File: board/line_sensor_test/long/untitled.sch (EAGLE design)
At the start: 12 parts

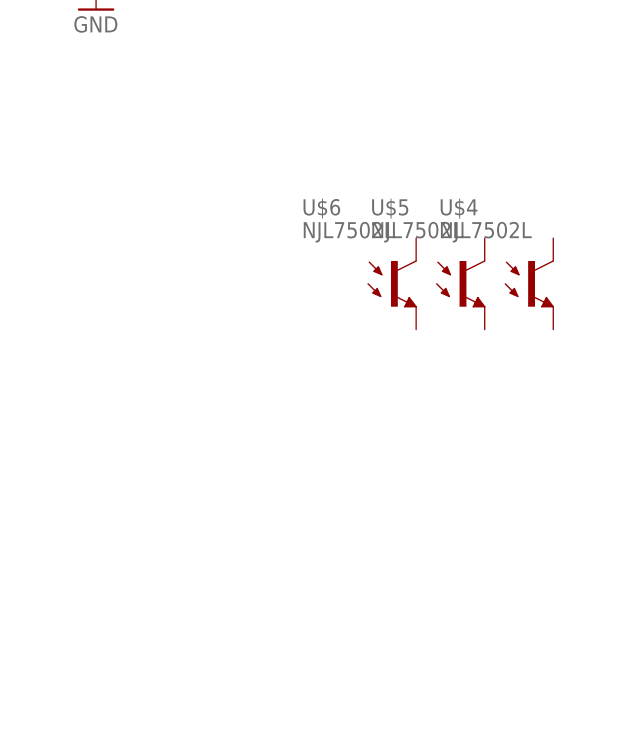
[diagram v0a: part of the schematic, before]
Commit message: add long line sensor
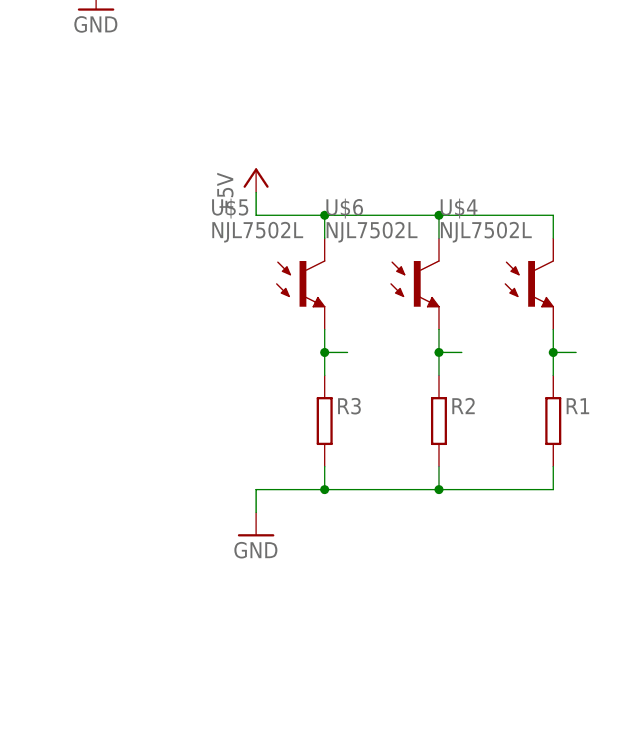
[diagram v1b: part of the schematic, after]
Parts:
- added R1, R2, R3: (no value), generic:RESISTOR1608
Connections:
- new net N$10: R1.1, U$4.E
- new net N$11: R3.1, U$5.E
- new net N$9: R2.1, U$6.E
- net +5V: now also U$4.C, U$5.C, U$6.C
- net GND: now also R1.2, R2.2, R3.2
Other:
- moved on the sheet: U$5, U$6
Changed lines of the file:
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@@
 <part name="LED6" library="adafruit" deviceset="WS2812B" device="_5050N"/>
 <part name="GND2" library="supply1" library_urn="urn:adsk.eagle:library:371" deviceset="GND" device=""/>
+<part name="R1" library="generic" deviceset="RESISTOR" device="1608"/>
+<part name="R2" library="generic" deviceset="RESISTOR" device="1608"/>
+<part name="R3" library="generic" deviceset="RESISTOR" device="1608"/>
+<part name="P+2" library="supply1" library_urn="urn:adsk.eagle:library:371" deviceset="+5V" device=""/>
+<part name="GND3" library="supply1" library_urn="urn:adsk.eagle:library:371" deviceset="GND" device=""/>
 </parts>
 <sheets>
@@
 <attribute name="VALUE" x="88.9" y="63.5" size="1.778" layer="96"/>
 </instance>
-<instance part="U$5" gate="G$1" x="91.44" y="58.42" smashed="yes">
-<attribute name="NAME" x="81.28" y="66.04" size="1.778" layer="95"/>
-<attribute name="VALUE" x="81.28" y="63.5" size="1.778" layer="96"/>
-</instance>
-<instance part="U$6" gate="G$1" x="83.82" y="58.42" smashed="yes">
-<attribute name="NAME" x="73.66" y="66.04" size="1.778" layer="95"/>
-<attribute name="VALUE" x="73.66" y="63.5" size="1.778" layer="96"/>
+<instance part="U$5" gate="G$1" x="73.66" y="58.42" smashed="yes">
+<attribute name="NAME" x="63.5" y="66.04" size="1.778" layer="95"/>
+<attribute name="VALUE" x="63.5" y="63.5" size="1.778" layer="96"/>
+</instance>
+<instance part="U$6" gate="G$1" x="86.36" y="58.42" smashed="yes">
+<attribute name="NAME" x="76.2" y="66.04" size="1.778" layer="95"/>
+<attribute name="VALUE" x="76.2" y="63.5" size="1.778" layer="96"/>
 </instance>
 <instance part="LED6" gate="G$1" x="-33.02" y="106.68" smashed="yes"/>
 <instance part="GND2" gate="1" x="50.8" y="88.9" smashed="yes">
 <attribute name="VALUE" x="48.26" y="86.36" size="1.778" layer="96"/>
+</instance>
+<instance part="R1" gate="G$1" x="101.6" y="43.18" smashed="yes">
+<attribute name="NAME" x="102.87" y="45.72" size="1.778" layer="95" font="vector" rot="MR180"/>
+<attribute name="VALUE" x="102.87" y="40.64" size="1.778" layer="96" font="vector"/>
+</instance>
+<instance part="R2" gate="G$1" x="88.9" y="43.18" smashed="yes">
+<attribute name="NAME" x="90.17" y="45.72" size="1.778" layer="95" font="vector" rot="MR180"/>
+<attribute name="VALUE" x="90.17" y="40.64" size="1.778" layer="96" font="vector"/>
+</instance>
+<instance part="R3" gate="G$1" x="76.2" y="43.18" smashed="yes">
+<attribute name="NAME" x="77.47" y="45.72" size="1.778" layer="95" font="vector" rot="MR180"/>
+<attribute name="VALUE" x="77.47" y="40.64" size="1.778" layer="96" font="vector"/>
+</instance>
+<instance part="P+2" gate="1" x="68.58" y="71.12" smashed="yes">
+<attribute name="VALUE" x="66.04" y="66.04" size="1.778" layer="96" rot="R90"/>
+</instance>
+<instance part="GND3" gate="1" x="68.58" y="30.48" smashed="yes">
+<attribute name="VALUE" x="66.04" y="27.94" size="1.778" layer="96"/>
 </instance>
 </instances>
@@
 <junction x="50.8" y="93.98"/>
 </segment>
+<segment>
+<pinref part="R1" gate="G$1" pin="2"/>
+<wire x1="101.6" y1="38.1" x2="101.6" y2="35.56" width="0.1524" layer="91"/>
+<wire x1="101.6" y1="35.56" x2="88.9" y2="35.56" width="0.1524" layer="91"/>
+<pinref part="R2" gate="G$1" pin="2"/>
+<wire x1="88.9" y1="35.56" x2="88.9" y2="38.1" width="0.1524" layer="91"/>
+<pinref part="R3" gate="G$1" pin="2"/>
+<wire x1="76.2" y1="38.1" x2="76.2" y2="35.56" width="0.1524" layer="91"/>
+<wire x1="76.2" y1="35.56" x2="88.9" y2="35.56" width="0.1524" layer="91"/>
+<junction x="88.9" y="35.56"/>
+<wire x1="76.2" y1="35.56" x2="68.58" y2="35.56" width="0.1524" layer="91"/>
+<junction x="76.2" y="35.56"/>
+<wire x1="68.58" y1="35.56" x2="68.58" y2="33.02" width="0.1524" layer="91"/>
+<pinref part="GND3" gate="1" pin="GND"/>
+</segment>
 </net>
 <net name="+5V" class="0">
@@
 <pinref part="P+1" gate="1" pin="+5V"/>
 </segment>
+<segment>
+<pinref part="U$4" gate="G$1" pin="C"/>
+<wire x1="101.6" y1="63.5" x2="101.6" y2="66.04" width="0.1524" layer="91"/>
+<wire x1="101.6" y1="66.04" x2="88.9" y2="66.04" width="0.1524" layer="91"/>
+<wire x1="88.9" y1="66.04" x2="76.2" y2="66.04" width="0.1524" layer="91"/>
+<wire x1="76.2" y1="66.04" x2="68.58" y2="66.04" width="0.1524" layer="91"/>
+<wire x1="68.58" y1="66.04" x2="68.58" y2="68.58" width="0.1524" layer="91"/>
+<pinref part="U$5" gate="G$1" pin="C"/>
+<wire x1="76.2" y1="63.5" x2="76.2" y2="66.04" width="0.1524" layer="91"/>
+<junction x="76.2" y="66.04"/>
+<pinref part="U$6" gate="G$1" pin="C"/>
+<wire x1="88.9" y1="63.5" x2="88.9" y2="66.04" width="0.1524" layer="91"/>
+<junction x="88.9" y="66.04"/>
+<pinref part="P+2" gate="1" pin="+5V"/>
+</segment>
 </net>
 <net name="N$1" class="0">
@@
 </segment>
 </net>
+<net name="N$9" class="0">
+<segment>
+<pinref part="U$6" gate="G$1" pin="E"/>
+<wire x1="88.9" y1="53.34" x2="88.9" y2="50.8" width="0.1524" layer="91"/>
+<wire x1="88.9" y1="50.8" x2="88.9" y2="48.26" width="0.1524" layer="91"/>
+<wire x1="88.9" y1="50.8" x2="91.44" y2="50.8" width="0.1524" layer="91"/>
+<junction x="88.9" y="50.8"/>
+<pinref part="R2" gate="G$1" pin="1"/>
+</segment>
+</net>
+<net name="N$10" class="0">
+<segment>
+<pinref part="U$4" gate="G$1" pin="E"/>
+<wire x1="101.6" y1="53.34" x2="101.6" y2="50.8" width="0.1524" layer="91"/>
+<wire x1="101.6" y1="50.8" x2="104.14" y2="50.8" width="0.1524" layer="91"/>
+<wire x1="101.6" y1="50.8" x2="101.6" y2="48.26" width="0.1524" layer="91"/>
+<junction x="101.6" y="50.8"/>
+<pinref part="R1" gate="G$1" pin="1"/>
+</segment>
+</net>
+<net name="N$11" class="0">
+<segment>
+<pinref part="U$5" gate="G$1" pin="E"/>
+<wire x1="76.2" y1="53.34" x2="76.2" y2="50.8" width="0.1524" layer="91"/>
+<wire x1="76.2" y1="50.8" x2="76.2" y2="48.26" width="0.1524" layer="91"/>
+<wire x1="76.2" y1="50.8" x2="78.74" y2="50.8" width="0.1524" layer="91"/>
+<junction x="76.2" y="50.8"/>
+<pinref part="R3" gate="G$1" pin="1"/>
+</segment>
+</net>

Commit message: 配線おわり
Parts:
- added JP2: 11PIN, jst_eph:11PIN
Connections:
- removed net N$10: R1.1, U$4.E
- removed net N$11: R3.1, U$5.E
- removed net N$4: LED1.A, LED2.A, LED3.A
- removed net N$8: LED4.VDD, LED5.VDD, LED6.VDD
- removed net N$9: R2.1, U$6.E
- new net LED_A: JP2.4, LED1.A, LED2.A, LED3.A
- new net LED_IN: JP2.6, LED6.DI
- new net LED_O: JP2.5, LED4.DO
- new net LINE1: JP2.9, R3.1, U$6.E
- new net LINE2: JP2.8, R2.1, U$5.E
- new net LINE3: JP2.7, R1.1, U$4.E
- new net LINE4: JP2.3, U$3.VOUT
- new net LINE5: JP2.2, U$2.VOUT
- new net LINE6: JP2.1, U$1.VOUT
- net +5V: now also JP2.10, LED4.VDD, LED5.VDD, LED6.VDD
- net GND: now also JP2.11
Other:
- moved on the sheet: R1, R2, R3, U$4, U$5, U$6
